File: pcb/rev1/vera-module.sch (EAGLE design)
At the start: 75 parts, among them J1 ICD15S13E4GX00LF, J2 RCJ-014, J3 HDR8X1, J4 C64CART, J5 BUS, Q1 BC847SOT-23, U1 ICE40UP5K-SG48ITR50, U2 MIC5504-3.3YM5-TR, U3 SN74CBTD3861PWR, U4 W25Q16JVSNIQ, U5 SG5032CAN_25.000000M-TJGA3, U6 74LVC4245APW, U8 AP3417CKTR-G1, U9 74AHCT1G14SE-7

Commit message: Finished work on rev1 VERA PCB.
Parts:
- removed Q1: BC847SOT-23, transistor:BC847SOT-23
- added C20, C21: 1u, rcl:CAPACITOR0603
- added C22, C24, C28: 4.7u, rcl:CAPACITOR0603
- added C27: 2.2u, rcl:CAPACITOR0603
- added C29, C30, C31: 100n, rcl:CAPACITOR0603
- added C3: 1n, rcl:CAPACITOR0603
- added J6: AUDIO, connectors:35RASMT2BHNTRX
- added J7: 2041021-3, connectors:2041021-3
- added J9: SERIAL, connectors:HDR4X1
- added R23: 470, rcl:RESISTOR0603
- added R24: 1k, rcl:RESISTOR0603
- added R29, R30, R31: CAY16-1001F4LF, rcl:RES_ARRAY41206
- added R32: 75, rcl:RESISTOR0603
- added R33, R36, R50, R52: 0, rcl:RESISTOR0603
- added R37: 1, rcl:RESISTOR0603
- added R38, R39: 560, rcl:RESISTOR0603
- added R42, R47, R48: 47k, rcl:RESISTOR0603
- added R49, R51: DNP, rcl:RESISTOR0603
- added R53, R54, R55, R56: 100, rcl:RESISTOR0603
- added U10: WM8524CGEDT, integrated_circuits:WM8524CGEDT
- added U11: 74AHC00PW, integrated_circuits:74AHC00PW
- added U12, U13: 74AHCT1G14SE-7, integrated_circuits:74AHCT1G14SE-7
- added U7: THS7314D, integrated_circuits:THS7314D
- C1: value 22p -> 100n
- C16: value 100n -> 2.7n
- C17: value 4.7u -> 2.7n
- C2: value 100n -> 10u; device rcl:CAPACITOR0603 -> rcl:CAPACITOR0805
- J4: value C64CART -> MD-40S; device connectors:C64CART -> connectors:MD-40S
- R25: value 1k -> 470
- R26, R27: value 1k -> 75
- R40: value 100 -> 47k
- R41: value 1 -> 47k
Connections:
- removed net BUS_RES#: U1.IOT_51A, U3.A2
- removed net COMPOSITE: J2.S, R26.1, R27.2
- new net AUDIO_BCK: U1.IOT_50B, U10.BCLK
- new net AUDIO_DATA: U1.IOT_51A, U10.DACDAT
- new net AUDIO_LRCK: U1.IOT_49A, U10.LRCLK
- new net BUS_PHY2_5V_IN: R50.1, U3.B1
- new net BUS_RDY_5V_OD: R52.1, U3.B2
- new net FLASH_SSEL_N: U11_3.Y, U4.CS#
- new net N$23: R32.1, U7.CH1_OUT
- new net N$24: C3.1, R33.2
- new net N$27: R29.2A, R30.2B
- new net N$28: R29.3A, R30.3B
- new net N$30: R29.4A, R30.4B
- new net N$31: R15.4A, R30.1A, R31.1B
- new net N$32: R30.2A, R31.1A, R31.2B
- new net N$33: R30.3A, R31.2A, R31.3B
- new net N$34: R24.1, R31.4A
- new net N$35: R30.4A, R31.3A, R31.4B
- new net N$36: R26.1, U7.CH2_OUT
- new net N$37: C1.2, C2.2, R36.1, U7.VCC
- new net N$38: C17.2, J6.TIP, R38.2
- new net N$39: C16.2, J6.RING, R39.2
- new net N$40: R38.1, U10.LINEVOUTL
- new net N$41: R39.1, U10.LINEVOUTR
- new net N$42: C20.1, U10.CPCA
- new net N$43: J7.DAT1, R47.2
- new net N$45: C21.2, U10.CPVOUTN
- new net N$46: U11_1.Y, U11_3.A
- new net N$47: U11_2.Y, U11_3.B, U11_4.B
- new net N$48: R49.1, U12.Y
- new net N$49: C27.2, U10.VMID
- new net N$50: R51.1, U13.Y
- new net N$51: J7.CMD/DI, R54.2
- new net N$52: J7.CLK/SCLK, R53.2
- new net N$53: J7.DAT3/CS, R56.2
- new net N$54: J7.DAT0/DO, R55.2
- new net SD_SSEL_N: R40.2, R56.1, U11_4.Y
- new net UART_RX: J9.2, U1.IOT_44B
- new net VIDEO_C: J4.4, R27.2
- new net VIDEO_CHROMA: R15.3B, R25.2, R7.3A, U7.CH3_IN
- new net VIDEO_COMP: C3.2, J2.S, R32.2
- new net VIDEO_LUMA: R14.1B, R23.2, R3.1A, U7.CH1_IN, U7.CH2_IN
- new net VIDEO_Y: J4.3, R26.2
- net +1.2V: now also U1.VCCPLL; no longer R41.2
- net +3.3V: now also C22.2, C24.2, C28.1, C29.2, J7.VDD, J9.1, R36.2, R40.1, R41.1, R42.1, R47.1, R48.1, U10.!MUTE, U10.AIFMODE, U10.AVDD, U10.LINEVDD, U11_PWR.VCC; no longer C2.1, Q1.C, R25.2
- net +5V: now also C30.2, C31.2, R37.1, U12.VCC, U13.VCC; no longer C25.2, J4.+5V@1, J4.+5V@2, U8.EN, U8.VIN
- net BUS_A0: now also U1.RGB2, U3.A3; no longer U1.IOT_48B, U3.A5
- net BUS_A0_5V: now also J5.17, U3.B3; no longer J4.A0, J5.15, U3.B5
- net BUS_A1: now also U1.RGB1, U3.A4; no longer U1.IOT_44B, U3.A6
- net BUS_A1_5V: now also J5.16, U3.B4; no longer J4.A1, J5.14, U3.B6
- net BUS_A2: now also U1.RGB0, U3.A5; no longer U1.IOT_43A, U3.A7
- net BUS_A2_5V: now also J5.15, U3.B5; no longer J4.A2, J5.13, U3.B7
- net BUS_CS#_5V: no longer J4.I/O1
- net BUS_D0_5V: no longer J4.D0
- net BUS_D1_5V: no longer J4.D1
- net BUS_D2_5V: no longer J4.D2
- net BUS_D3_5V: no longer J4.D3
- net BUS_D4_5V: no longer J4.D4
- net BUS_D5_5V: no longer J4.D5
- net BUS_D6_5V: no longer J4.D6
- net BUS_D7_5V: no longer J4.D7
- net BUS_IRQ#: now also U1.IOT_43A, U3.A6; no longer U1.IOT_49A, U3.A1
- net BUS_IRQ#_5V: now also J5.14, U3.B6; no longer J4.!IRQ, J5.19, U3.B1
- net BUS_PHY2: now also U12.A, U3.A1; no longer U3.A4
- net BUS_PHY2_5V: now also J5.18, R49.2, R50.2; no longer J4.S02, J5.16, U3.B4
- net BUS_RDY: now also J9.3, U1.IOT_48B, U13.A, U3.A2; no longer U1.IOT_50B, U3.A3
- net BUS_RDY_5V: now also J5.19, R51.2, R52.2; no longer J5.17, U3.B3
- net BUS_RES#_5V: now also J5.12, U3.B8; no longer J4.!RESET, J5.18, U3.B2
- net BUS_RW#: now also U3.A7; no longer U3.A8
- net BUS_RW#_5V: now also J5.13, U3.B7; no longer J4.R/!W, J5.12, U3.B8
- net FPGA_CDONE: now also U11_1.A, U11_1.B, U11_4.A
- net FPGA_CRESET_B: now also U3.A8
- net GND: now also C2.1, C21.1, C22.1, C24.1, C27.1, C28.2, C29.1, C30.1, C31.1, J1.MH1, J1.MH2, J4.1, J4.2, J4.MH, J6.SLEEVE, J7.MP1, J7.MP2, J7.MP3, J7.MP4, J7.VSS1, J7.VSS2, J9.4, R23.1, R24.2, R25.1, U10.AGND, U10.LINEGND, U11_PWR.GND, U12.GND, U13.GND, U7.GND; no longer C2.2, J4.GND@1, J4.GND@2, J4.GND@3, J4.GND@4, R27.1
- net N$12: now also R27.1, R33.1, U7.CH3_OUT; no longer C1.2, Q1.B, R14.1B, R25.1, R3.1A
- net N$22: now also C25.2, R37.2, U8.EN, U8.VIN; no longer R15.2A, R15.3B, R7.3A
- net N$26: now also C20.2, U10.CPCB; no longer Q1.E, R26.2
- net N$29: now also R15.2A; no longer R15.4A
- net N$44: now also J7.DAT2, R48.2; no longer R40.1, U1.VCCPLL
- net N$9: now also R29.1A, R30.1B; no longer C16.2, C17.2, R40.2, R41.1
- net SPI_MISO: now also R42.2, R55.1
- net SPI_MOSI: now also R41.2, R54.1
- net SPI_SCK: now also R53.1
- net SPI_SSEL_N: now also U11_2.A, U11_2.B; no longer U4.CS#
- net SYSCLK: now also U10.MCLK
- net VGA_B0: now also R29.4B
- net VGA_B1: now also R29.3B
- net VGA_B2: now also R29.2B
- net VGA_B3: now also R29.1B
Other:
- note added: "Audio output"
- note added: "Bus connector"
- note added: "Optional level conversion for PHY2 + RDY"
- note added: "SPI pins multiplexing"
- note added: "Secure Digital Interface"
- note removed: "Bus connectors"

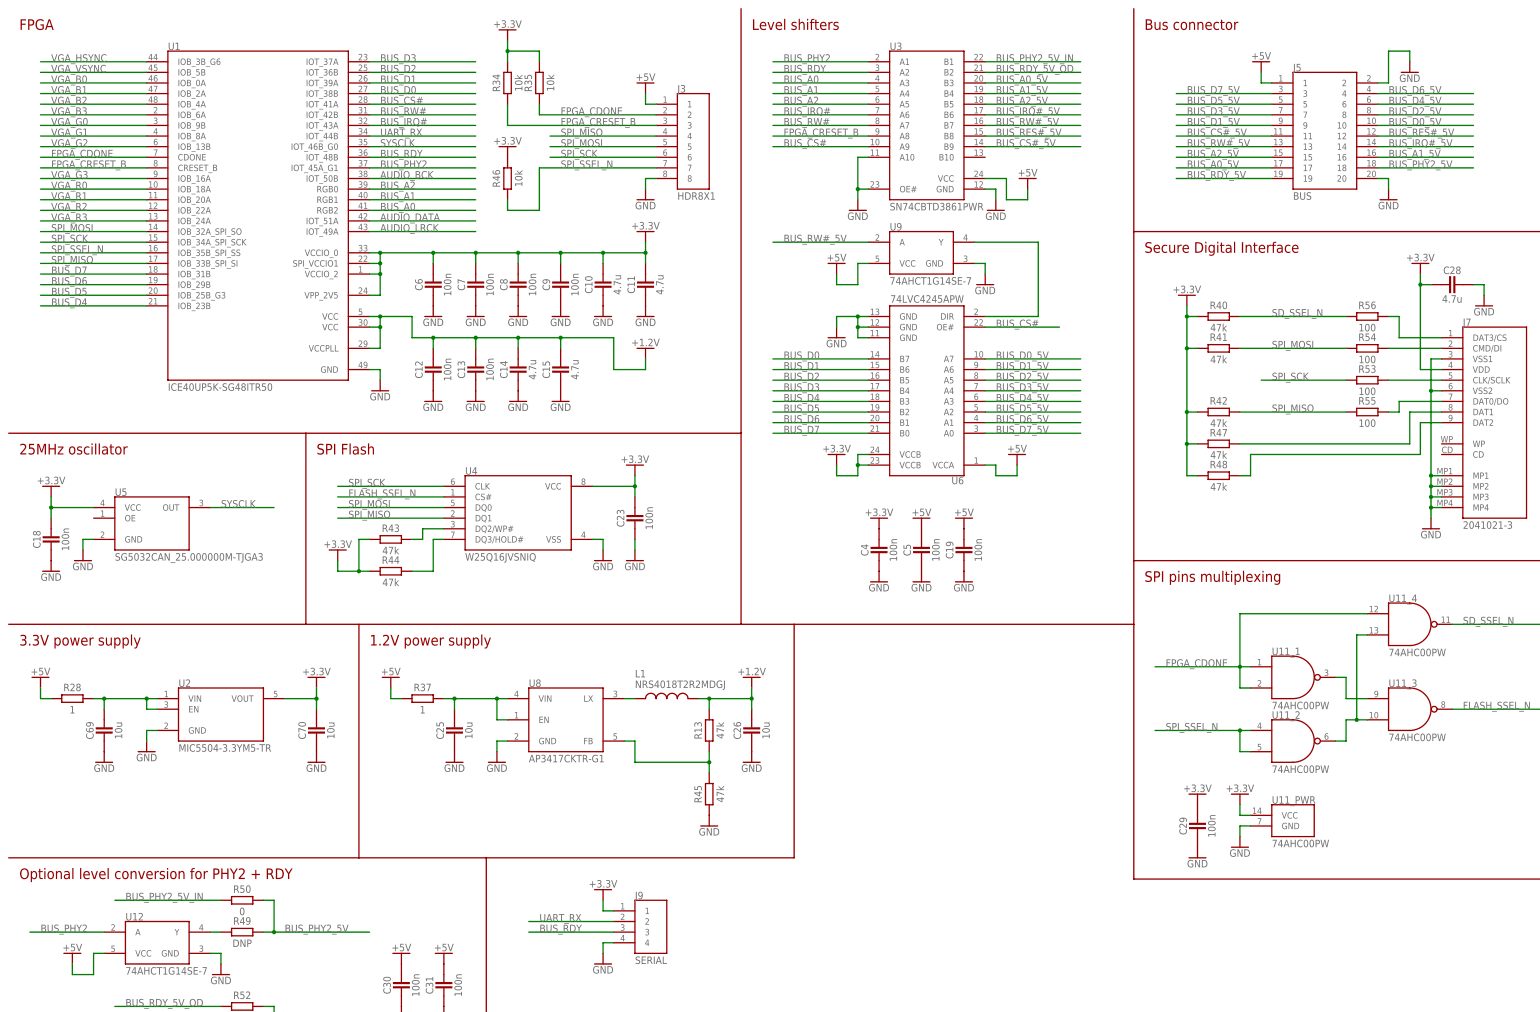
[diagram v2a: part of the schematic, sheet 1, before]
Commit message: Renamed PHY2 to PHI2. Added missing inits on reset.
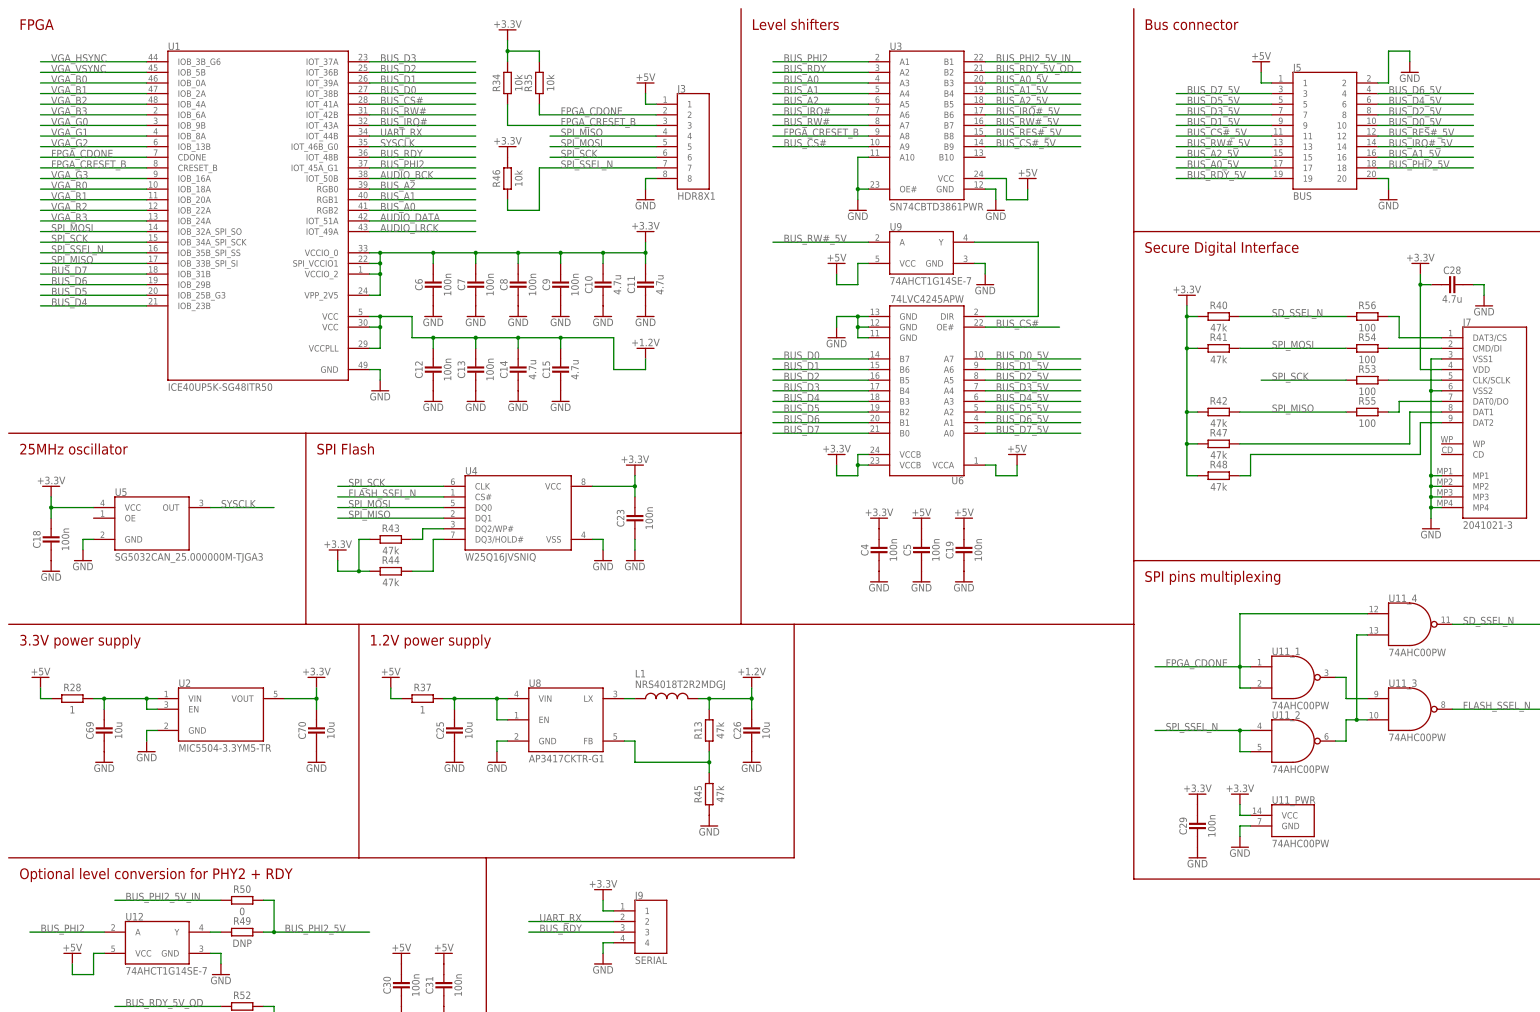
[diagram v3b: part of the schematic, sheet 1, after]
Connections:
- net BUS_PHY2 renamed BUS_PHI2
- net BUS_PHY2_5V renamed BUS_PHI2_5V
- net BUS_PHY2_5V_IN renamed BUS_PHI2_5V_IN
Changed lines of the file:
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@@
 </segment>
 </net>
-<net name="BUS_PHY2" class="0">
+<net name="BUS_PHI2" class="0">
 <segment>
 <pinref part="U1" gate="_" pin="IOT_45A_G1"/>
@@
 </segment>
 </net>
-<net name="BUS_PHY2_5V" class="0">
+<net name="BUS_PHI2_5V" class="0">
 <segment>
 <wire x1="86.36" y1="55.88" x2="63.5" y2="55.88" width="0.1524" layer="91"/>
@@
 </segment>
 </net>
-<net name="BUS_PHY2_5V_IN" class="0">
+<net name="BUS_PHI2_5V_IN" class="0">
 <segment>
 <wire x1="256.54" y1="264.16" x2="233.68" y2="264.16" width="0.1524" layer="91"/>
